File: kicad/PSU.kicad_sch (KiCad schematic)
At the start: 66 parts, among them J1 +12V in1, J10 0V, J11 +5Vu, J2 +12V in2, J3 0v, J4 Conn_02x20_Odd_Even, J5 LED-, J6 LED+, J7 Sw, J8 Sw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

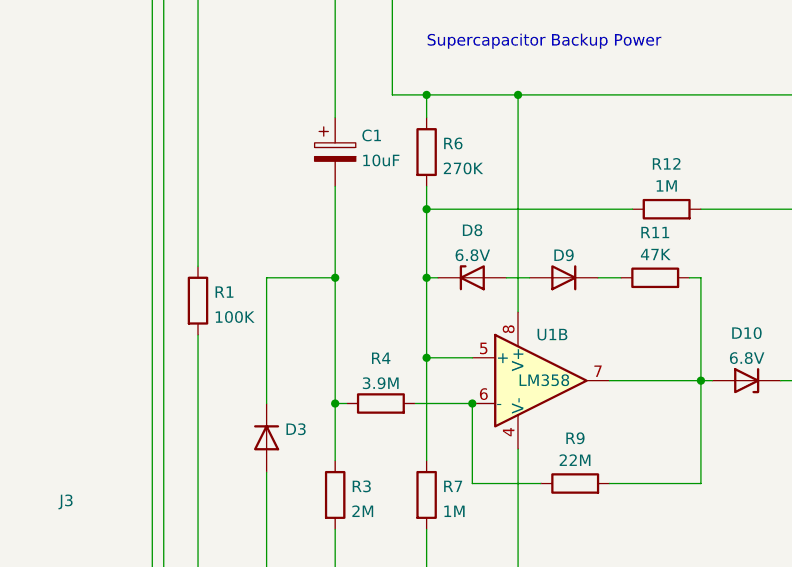
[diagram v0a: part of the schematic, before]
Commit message: Initial release of revision 2.  Fixes from prototyping and experiments.
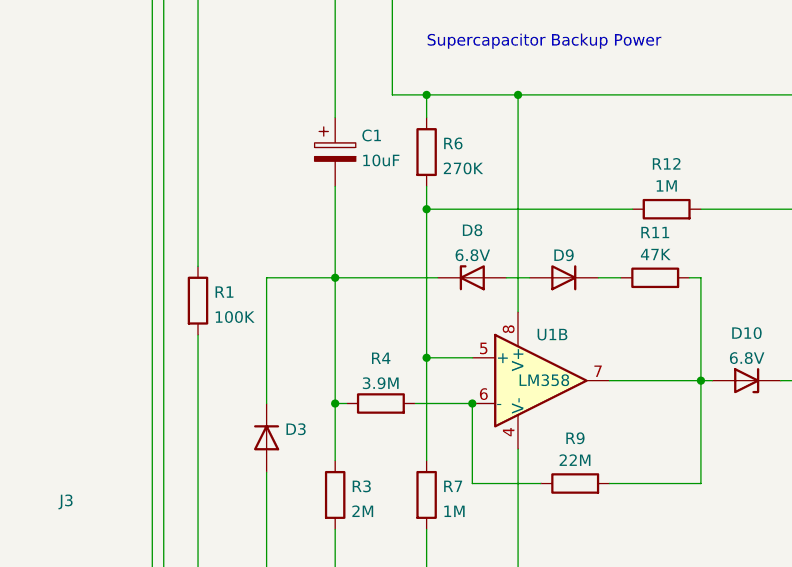
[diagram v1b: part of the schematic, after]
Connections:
- net at C1.2, D3.1 (K), R3.1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: now also D8.1 (K)
- net at R12.1, R6.2, R7.1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: no longer D8.1 (K)
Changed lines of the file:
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@@
   (junction (at 115.57 85.09) (diameter 0) (color 0 0 0 0)
-  )
-  (junction (at 57.15 92.71) (diameter 0) (color 0 0 0 0)
   )
   (junction (at 66.04 162.56) (diameter 0) (color 0 0 0 0)
@@
     (stroke (width 0) (type default) (color 0 0 0 0))
   )
-  (wire (pts (xy 57.15 92.71) (xy 57.15 101.6))
-    (stroke (width 0) (type default) (color 0 0 0 0))
-  )
   (wire (pts (xy 147.32 105.41) (xy 147.32 113.03))
     (stroke (width 0) (type default) (color 0 0 0 0))
@@
     (stroke (width 0) (type default) (color 0 0 0 0))
   )
+  (wire (pts (xy 58.42 92.71) (xy 46.99 92.71))
+    (stroke (width 0) (type default) (color 0 0 0 0))
+  )
   (wire (pts (xy 154.94 41.91) (xy 161.29 41.91))
     (stroke (width 0) (type default) (color 0 0 0 0))
@@
     (stroke (width 0) (type default) (color 0 0 0 0))
   )
-  (wire (pts (xy 57.15 85.09) (xy 57.15 92.71))
+  (wire (pts (xy 57.15 85.09) (xy 57.15 101.6))
     (stroke (width 0) (type default) (color 0 0 0 0))
   )
@@
     (stroke (width 0) (type default) (color 0 0 0 0))
   )
-  (wire (pts (xy 58.42 92.71) (xy 57.15 92.71))
-    (stroke (width 0) (type default) (color 0 0 0 0))
-  )
